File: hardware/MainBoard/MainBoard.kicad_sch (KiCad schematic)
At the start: 0 parts

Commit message: MainBoard作った(未：回転数計、他)
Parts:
- added A1: RaspberryPi_Pico, Module:RaspberryPi_Pico_Common_Unspecified, symbol MCU_Module:RaspberryPi_Pico
- added J1: MPU9250, symbol Connector_Generic:Conn_01x10
- added J2: Micro_SD_Card, symbol Connector:Micro_SD_Card
- added J3: Servo, symbol Connector_Generic:Conn_01x03
- added J4: Relay, symbol Connector_Generic:Conn_01x03
- added J5: MotorDriver, symbol Connector_Generic:Conn_01x05
- added J6: PicoBATT+, symbol Connector_Generic:Conn_01x02
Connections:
- new net: A1.39 (VSYS), J6.1 (Pin_1)
- new net: A1.13 (GND), A1.18 (GND), A1.23 (GND), A1.28 (GND), A1.3 (GND), A1.38 (GND), A1.8 (GND)
- new net ADO: J1.7 (Pin_7)
- new net CLK: A1.24 (GPIO18), J2.5 (CLK)
- new net CS: A1.22 (GPIO17), J2.2 (DAT3/CD)
- new net ECL: J1.6 (Pin_6)
- new net EDA: J1.5 (Pin_5)
- new net FSYNC: J1.10 (Pin_10)
- new net GND: J1.2 (Pin_2), J2.6 (VSS), J3.1 (Pin_1), J4.1 (Pin_1), J5.1 (Pin_1), J6.2 (Pin_2)
- new net IN1: A1.15 (GPIO11), J5.5 (Pin_5)
- new net IN2: A1.16 (GPIO12), J5.4 (Pin_4)
- new net IN3: A1.17 (GPIO13), J5.3 (Pin_3)
- new net IN4: A1.19 (GPIO14), J5.2 (Pin_2)
- new net INT: J1.8 (Pin_8)
- new net MISO: A1.21 (GPIO16), J2.7 (DAT0)
- new net MOSI: A1.25 (GPIO19), J2.3 (CMD)
- new net NCS: J1.9 (Pin_9)
- new net Relay_S: A1.20 (GPIO15), J4.3 (Pin_3)
- new net SCL: A1.7 (GPIO5), J1.3 (Pin_3)
- new net SDA: A1.6 (GPIO4), J1.4 (Pin_4)
- new net Servo_S: A1.14 (GPIO10), J3.3 (Pin_3)
- new net VDD: A1.36 (3V3), J1.1 (Pin_1), J2.4 (VDD), J4.2 (Pin_2)
- no-connect marks 0 -> 18

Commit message: ちょっと修正
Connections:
- net GND: now also A1.13 (GND), A1.18 (GND), A1.23 (GND), A1.28 (GND), A1.3 (GND), A1.38 (GND), A1.8 (GND)
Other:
- moved on the sheet: J1, J4, J5

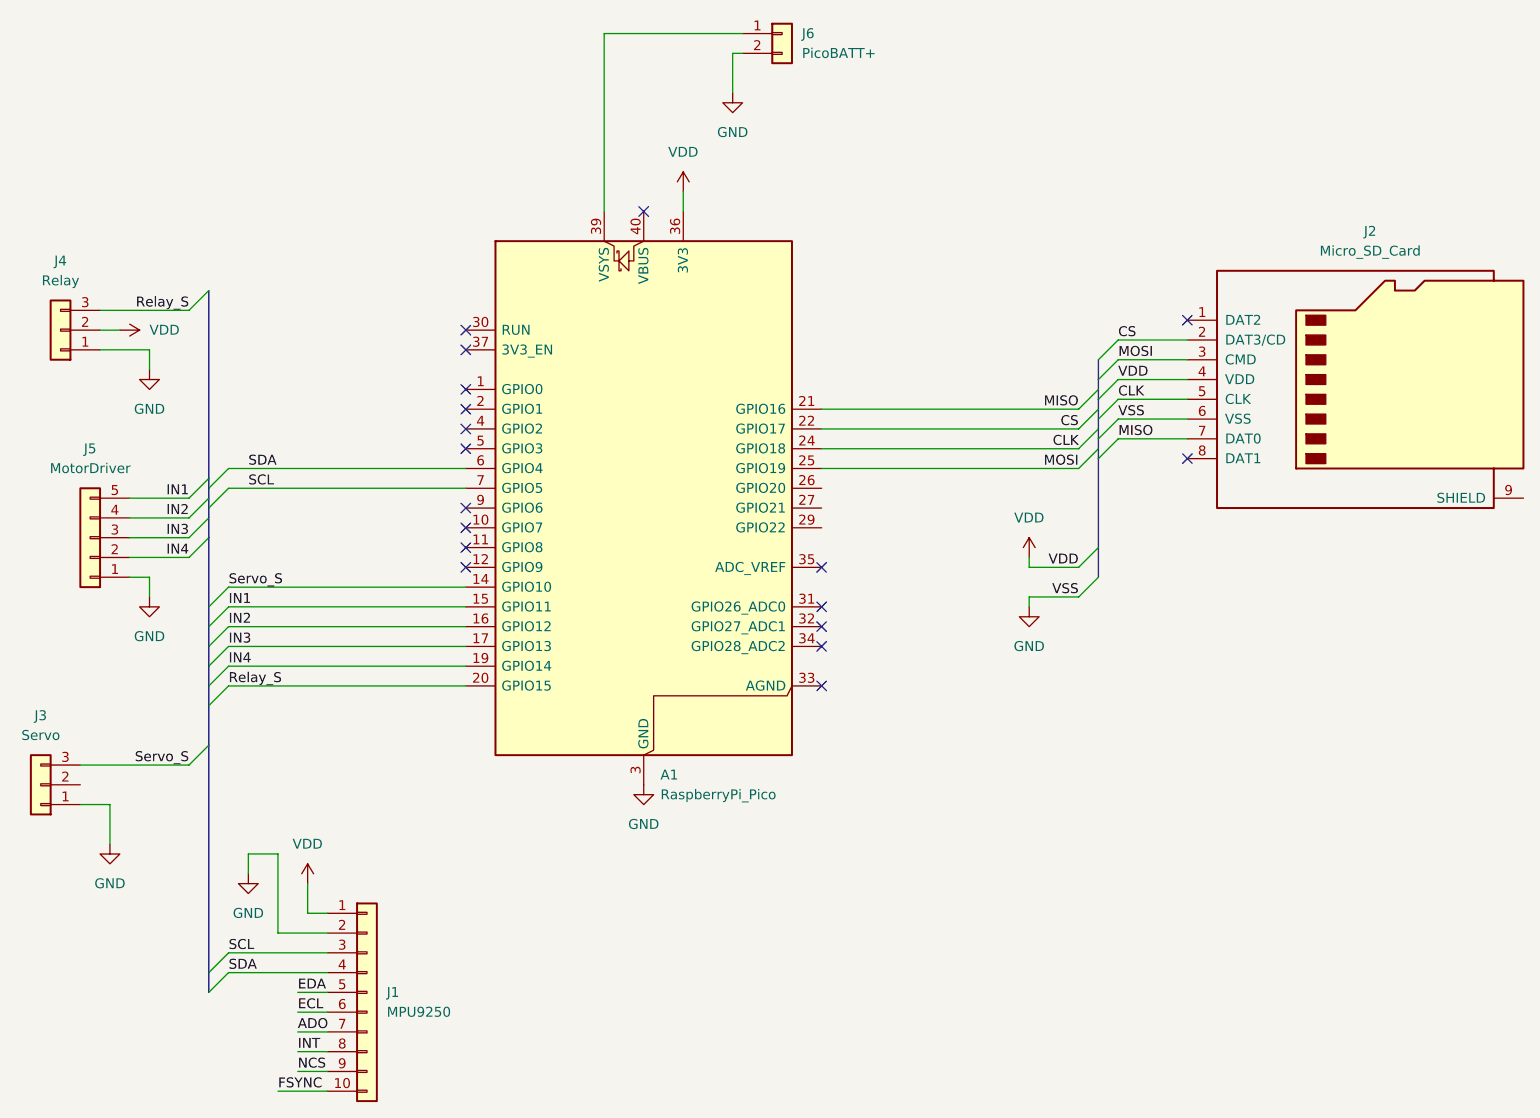
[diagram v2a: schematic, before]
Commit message: 回転数計を追加。サーボの電源をVCCから引いてみた。
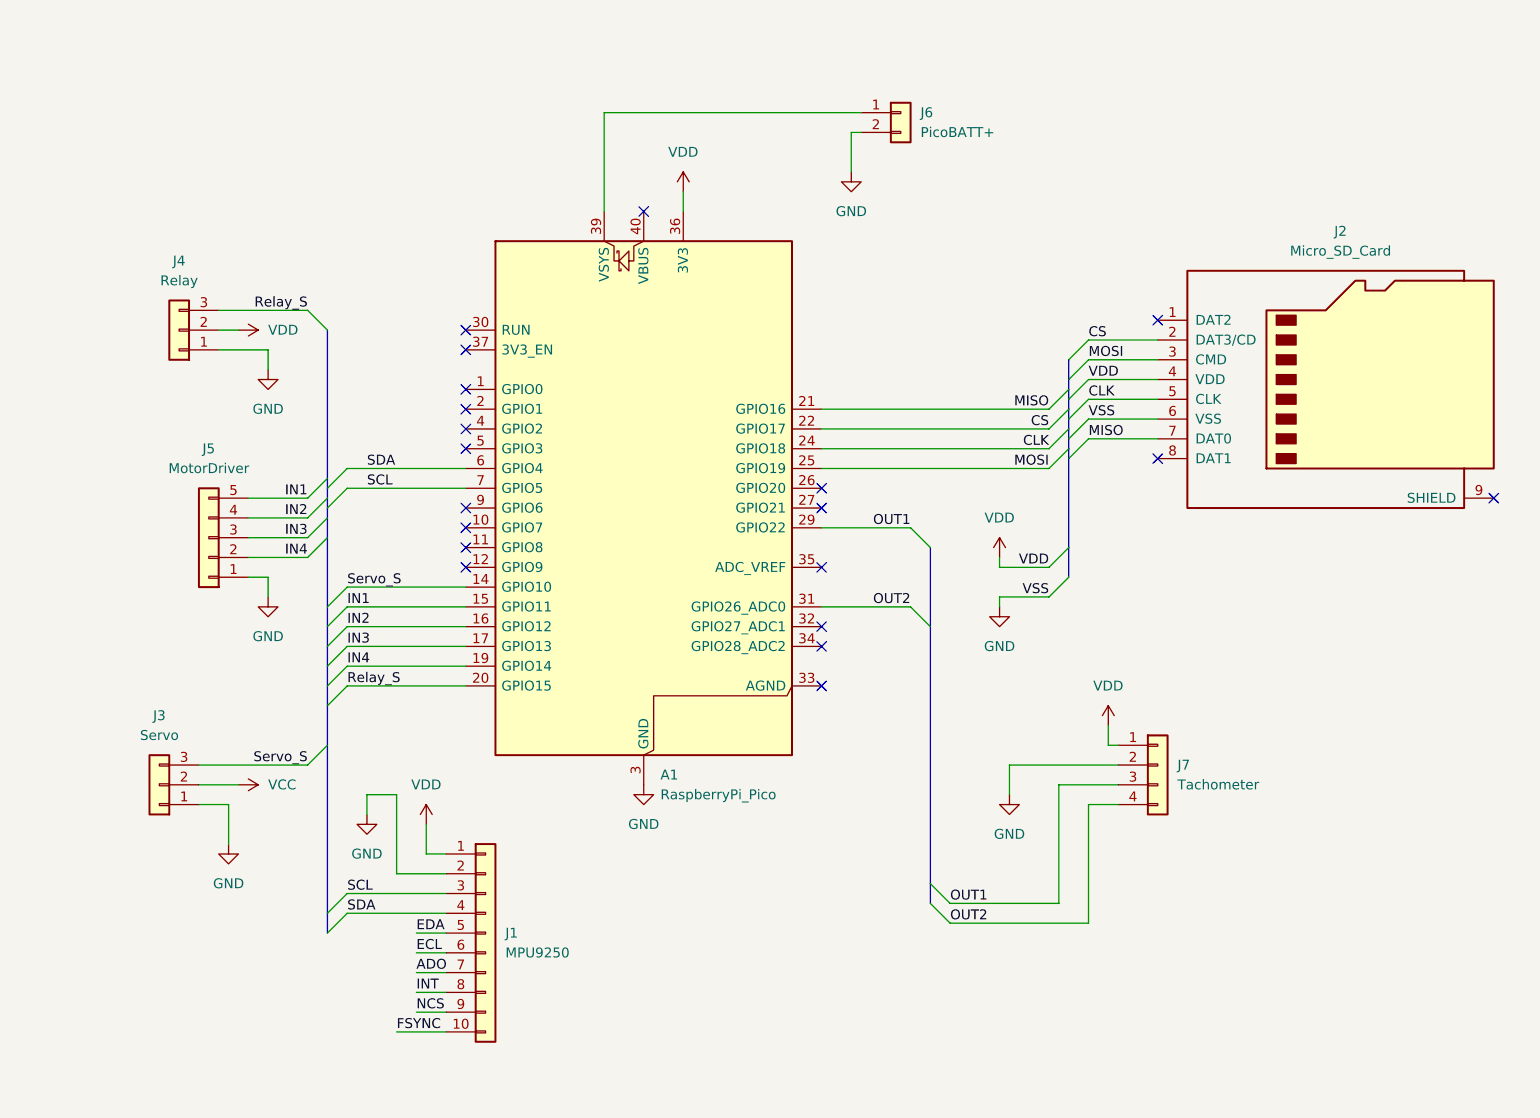
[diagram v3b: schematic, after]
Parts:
- added J7: Tachometer, symbol Connector_Generic:Conn_01x04
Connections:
- net GND: now also J7.2 (Pin_2)
- net VDD: now also J7.1 (Pin_1)
- net VCC: now reaches J3.2 (Pin_2)
- net OUT1: now reaches A1.29 (GPIO22)
- net OUT1: now also J7.3 (Pin_3)
- net OUT2: now reaches A1.31 (GPIO26_ADC0)
- net OUT2: now also J7.4 (Pin_4)
- no-connect marks 18 -> 20
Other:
- moved on the sheet: J1, J2, J3, J4, J5, J6
